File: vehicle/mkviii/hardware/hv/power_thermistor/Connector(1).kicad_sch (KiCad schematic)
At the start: 1 part, among them J1 T2M-110-01-X-D-TH-WT

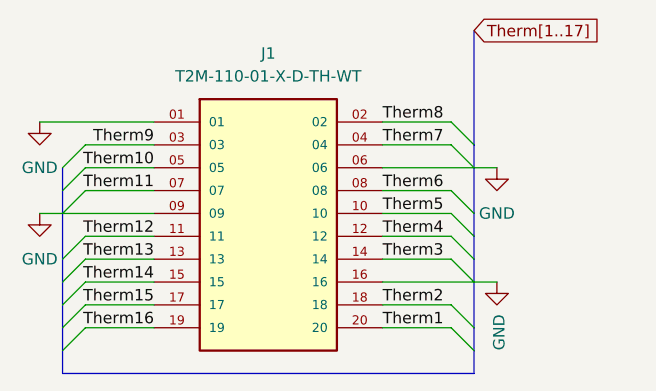
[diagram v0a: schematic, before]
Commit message: Power Therm overhall, have not been reviewed yet
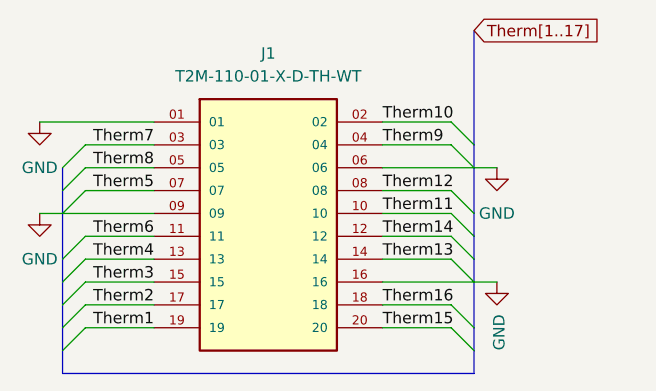
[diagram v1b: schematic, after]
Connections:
- net Therm1: now also J1.19; no longer J1.20
- net Therm10: now also J1.02; no longer J1.05
- net Therm11: now also J1.10; no longer J1.07
- net Therm12: now also J1.08; no longer J1.11
- net Therm13: now also J1.14; no longer J1.13
- net Therm14: now also J1.12; no longer J1.15
- net Therm15: now also J1.20; no longer J1.17
- net Therm16: now also J1.18; no longer J1.19
- net Therm2: now also J1.17; no longer J1.18
- net Therm3: now also J1.15; no longer J1.14
- net Therm4: now also J1.13; no longer J1.12
- net Therm5: now also J1.07; no longer J1.10
- net Therm6: now also J1.11; no longer J1.08
- net Therm7: now also J1.03; no longer J1.04
- net Therm8: now also J1.05; no longer J1.02
- net Therm9: now also J1.04; no longer J1.03
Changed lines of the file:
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@@
 		)
 	)
-	(label "Therm13"
+	(label "Therm4"
 		(at 43.18 50.8 180)
 		(effects
@@
 		)
 	)
-	(label "Therm4"
+	(label "Therm14"
 		(at 68.58 48.26 0)
 		(effects
@@
 		)
 	)
-	(label "Therm14"
+	(label "Therm3"
 		(at 43.18 53.34 180)
 		(effects
@@
 		)
 	)
-	(label "Therm3"
+	(label "Therm13"
 		(at 68.58 50.8 0)
 		(effects
@@
 		)
 	)
-	(label "Therm11"
+	(label "Therm5"
 		(at 43.18 43.18 180)
 		(effects
@@
 		)
 	)
-	(label "Therm16"
+	(label "Therm1"
 		(at 43.18 58.42 180)
 		(effects
@@
 		)
 	)
-	(label "Therm12"
+	(label "Therm6"
 		(at 43.18 48.26 180)
 		(effects
@@
 		)
 	)
-	(label "Therm2"
+	(label "Therm16"
 		(at 68.58 55.88 0)
 		(effects
@@
 		)
 	)
-	(label "Therm7"
+	(label "Therm9"
 		(at 68.58 38.1 0)
 		(effects
@@
 		)
 	)
-	(label "Therm1"
+	(label "Therm15"
 		(at 68.58 58.42 0)
 		(effects
@@
 		)
 	)
-	(label "Therm15"
+	(label "Therm2"
 		(at 43.18 55.88 180)
 		(effects
@@
 		)
 	)
-	(label "Therm5"
+	(label "Therm11"
 		(at 68.58 45.72 0)
 		(effects
@@
 		)
 	)
-	(label "Therm6"
+	(label "Therm12"
 		(at 68.58 43.18 0)
 		(effects
@@
 		)
 	)
-	(label "Therm9"
+	(label "Therm7"
 		(at 43.18 38.1 180)
 		(effects
@@
 		)
 	)
-	(label "Therm10"
+	(label "Therm8"
 		(at 43.18 40.64 180)
 		(effects
@@
 		)
 	)
-	(label "Therm8"
+	(label "Therm10"
 		(at 68.58 35.56 0)
 		(effects

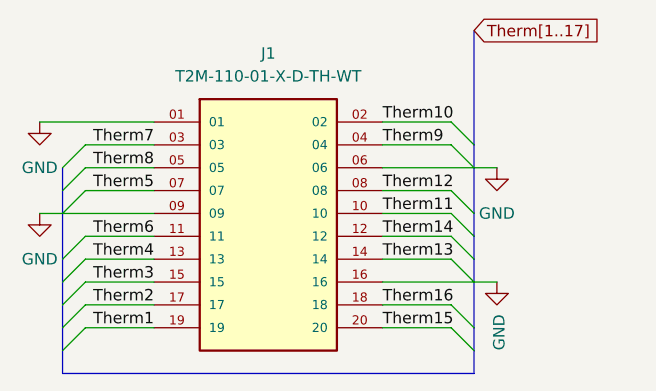
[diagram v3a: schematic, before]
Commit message: fixes for connector to BMS MOBO
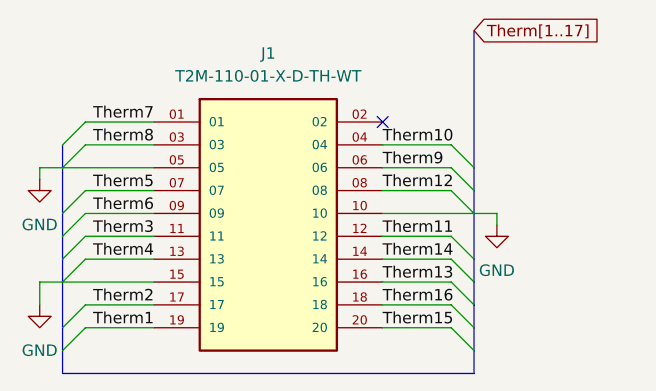
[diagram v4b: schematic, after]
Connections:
- net GND: now also J1.05, J1.10, J1.15; no longer J1.01, J1.06, J1.09, J1.16
- net Therm10: now also J1.04; no longer J1.02
- net Therm11: now also J1.12; no longer J1.10
- net Therm13: now also J1.16; no longer J1.14
- net Therm14: now also J1.14; no longer J1.12
- net Therm3: now also J1.11; no longer J1.15
- net Therm6: now also J1.09; no longer J1.11
- net Therm7: now also J1.01; no longer J1.03
- net Therm8: now also J1.03; no longer J1.05
- net Therm9: now also J1.06; no longer J1.04
- no-connect marks 0 -> 1
